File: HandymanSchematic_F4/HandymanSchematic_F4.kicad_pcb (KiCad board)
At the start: 4 copper layers, 60.5 x 94.5 mm, 81 parts, among them J1 SWD Header, J2 Footswitch, J3 TunerIn, J4 TuneThru, J5 GateIn, J6 GateOut, J7 PowerJack, Q1 BC847, Q2 2N7002, Q3 2N7002, SW1 RST, SW2 BYP, U1 SH1106, U2 TL074, U3 STM32F411RETx, U4 AMS1117, U6 TL072, Y1 16MHz

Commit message: noise schematic tweaks
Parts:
- removed R25: 100k, Resistor_SMD:R_0805_2012Metric
- removed U6: TL072, Package_SO:SOIC-8_3.9x4.9mm_P1.27mm
- added C2: 10u, Capacitor_SMD:C_0805_2012Metric, F.Cu at (88.9, 24.1)
- added C25: 2n2, Capacitor_SMD:C_0805_2012Metric, F.Cu at (88.9, 30.1)
- added C26: 470u, Capacitor_THT:CP_Radial_D6.3mm_P2.50mm, F.Cu at (100.9, 26.5)
- added C9: 10u, Capacitor_SMD:C_0805_2012Metric, F.Cu at (88.9, 27.1)
- added D2: BAT54S, Package_TO_SOT_SMD:SOT-23, F.Cu at (93.6, 24.8)
- added R11: 220, Resistor_SMD:R_0805_2012Metric, F.Cu at (84.5, 30.0)
- added R30: 1Meg, Resistor_SMD:R_0805_2012Metric, F.Cu at (84.5, 32.9)
- added R38: 470k, Resistor_SMD:R_0805_2012Metric, F.Cu at (84.5, 35.9)
- added R39: 4k7, Resistor_SMD:R_0805_2012Metric, F.Cu at (84.5, 38.8)
- added R4: 220, Resistor_SMD:R_0805_2012Metric, F.Cu at (84.5, 24.1)
- added R40: 22, Resistor_SMD:R_0805_2012Metric, F.Cu at (100.2, 31.9)
- added R6: 220, Resistor_SMD:R_0805_2012Metric, F.Cu at (84.5, 27.0)
- added U5: LM2904, Package_SO:SOIC-8_3.9x4.9mm_P1.27mm, F.Cu at (25.4, 13.7)
- R12, R8: value 470k -> 1Meg
- R13, R26: value 470k -> 100k
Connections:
- C1 pad 1: +9V -> +9VA
- C3 pad 1: +9V -> +9VA
- D4 pad 1: /Analog/AmpCathode -> Net-(D4-K)
- D7 pad 2: /Analog/AmpAnode -> Net-(D7-A)
- R1 pad 1: +9V -> +9VA
- R22 pad 2: Net-(C10-Pad1) -> Net-(R11-Pad1)
- R26 pad 2: TUNE_ADC -> Net-(R26-Pad2)
- R5 pad 1: +9V -> +9VA
- U2 pad 4: +9V -> +9VA
- U2 pad 8: Net-(C10-Pad1) -> Net-(R11-Pad1)

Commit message: layout
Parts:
- C26: moved to B.Cu
- moved D2 83.6 mm to (12.4, 4.80)
- moved C25 75.5 mm to (16.7, 8.03), turned to -90 degrees
- moved R39 71.2 mm to (20.3, 7.97), turned to 90 degrees
- moved R30 68.1 mm to (18.8, 15.1), turned to 90 degrees
- moved C2 66.6 mm to (22.5, 18.7), turned to -90 degrees
- moved R40 66.2 mm to (41.4, 1.70), turned to 90 degrees
- moved R38 65.3 mm to (22.5, 15.1), turned to 90 degrees
- moved R4 65.2 mm to (19.3, 26.5)
- moved C26 63.3 mm to (41.4, 4.95)
- moved R11 62.0 mm to (22.9, 37.0), turned to -90 degrees
- moved C9 59.8 mm to (29.8, 18.1), turned to -90 degrees
- moved R6 51.7 mm to (32.9, 23.6)
- moved R24 37.3 mm to (15.3, 15.0), turned to -90 degrees
- moved R28 31.4 mm to (16.7, 11.5), turned to -90 degrees
- moved R22 4.60 mm to (19.5, 33.6), turned to 0 degrees
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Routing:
- net +3.3V: track 290.6 -> 0.00 mm, vias 4 -> 0
- net +9V: track 157.3 -> 0.00 mm, vias 4 -> 0
- net /Digital/TunerModeIn: track 103.4 -> 0.00 mm, vias 2 -> 0
- net TUNE_IN: track 82.6 -> 0.00 mm, vias 1 -> 0
- net CLOSED_OUT: track 77.5 -> 0.00 mm, vias 2 -> 0
- net /Analog/VG: track 71.6 -> 0.00 mm, vias 2 -> 0
- net TUNE_THRU: track 58.9 -> 0.00 mm, vias 1 -> 0
- net Net-(C2-Pad1): track 55.3 -> 0.00 mm, vias 2 -> 0
- net NRST: track 46.6 -> 0.00 mm, vias 1 -> 0
- net LOOP_IN: track 40.5 -> 0.00 mm
- net /Digital/GateByp: track 36.5 -> 0.00 mm, vias 1 -> 0
- net RELEASE_IN: track 36.4 -> 0.00 mm, vias 1 -> 0
- net Net-(C11-Pad1): track 30.2 -> 0.00 mm
- net THRESH_IN: track 29.7 -> 0.00 mm, vias 1 -> 0
- net TUNE_ADC: track 27.8 -> 0.00 mm, vias 1 -> 0
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
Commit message: prelim routing
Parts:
- moved C9 0.93 mm to (28.9, 18.1)
- moved R19 0.36 mm to (16.0, 35.6), turned to 0 degrees
- moved C14 0.36 mm to (16.0, -4.65)
- moved R310 0.27 mm to (19.6, 3.30)
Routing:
- net +3.3V: track 0.00 -> 222.5 mm, vias 0 -> 6
- net /Digital/TunerModeIn: track 0.00 -> 92.0 mm, vias 0 -> 1
- net +9VA: track 0.00 -> 89.2 mm, vias 0 -> 2
- net TUNE_IN: track 0.00 -> 80.3 mm, vias 0 -> 1
- net CLOSED_OUT: track 0.00 -> 67.9 mm, vias 0 -> 2
- net /Analog/VG: track 0.00 -> 64.3 mm, vias 0 -> 3
- net +9V: track 0.00 -> 64.2 mm, vias 0 -> 2
- net TUNE_THRU: track 0.00 -> 55.9 mm
- net LOOP_IN: track 0.00 -> 55.5 mm
- net NRST: track 0.00 -> 48.0 mm, vias 0 -> 1
- net RELEASE_IN: track 0.00 -> 42.9 mm, vias 0 -> 1
- net +3.3VA: track 0.00 -> 42.5 mm, vias 0 -> 2
- net /Digital/GateByp: track 0.00 -> 36.1 mm, vias 0 -> 2
- net THRESH_IN: track 0.00 -> 35.0 mm, vias 0 -> 1
- net /Analog/SumPt: track 0.00 -> 30.3 mm, vias 0 -> 2
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
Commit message: wider jack spacing, DRC passing
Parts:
- moved J8 0.34 mm to (53.0, 13.9)
- moved J4 0.28 mm to (18.5, 22.7)
- moved J6 0.28 mm to (18.5, 43.8)
- moved J3 0.15 mm to (37.2, 38.9)
- moved J5 0.15 mm to (37.2, 60.0)
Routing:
- net LOOP_IN: track 55.5 -> 53.6 mm
- net GND: vias 63 -> 69

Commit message: stitching vias, trace improvements
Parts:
- moved C11 0.37 mm to (40.6, 36.6)
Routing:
- net TUNE_IN: track 80.3 -> 85.6 mm
- net NRST: track 48.0 -> 51.5 mm
- net /Analog/AmpCathode: track 19.5 -> 17.5 mm, vias 2 -> 0
- net TUNE_THRU: track 55.9 -> 54.3 mm
- net /Digital/DISP_SDA: track 26.5 -> 27.7 mm
- net /Digital/TunerModeIn: track 91.8 -> 92.4 mm
- net /Digital/GateByp: track 36.1 -> 36.3 mm, vias 2 -> 1
- net GND: vias 69 -> 74

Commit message: rev7 ready for fab
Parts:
- moved R3 8.95 mm to (53.0, 26.9)
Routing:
- net +9VA: track 89.1 -> 73.8 mm, vias 2 -> 3
- net THRESH_IN: track 35.0 -> 29.7 mm
- net NRST: track 51.5 -> 49.8 mm
- net CLOSED_OUT: track 67.9 -> 69.5 mm
- net +9V: track 64.2 -> 65.6 mm
- net Net-(Q1-B): track 7.67 -> 6.61 mm
- net +3.3VA: track 42.5 -> 43.1 mm
- net GND: vias 74 -> 80
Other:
- board text added: "Rev 7- 10/2026 Hayden Setlik"
- board text removed: "Rev 6- 08/2026 Hayden Setlik"

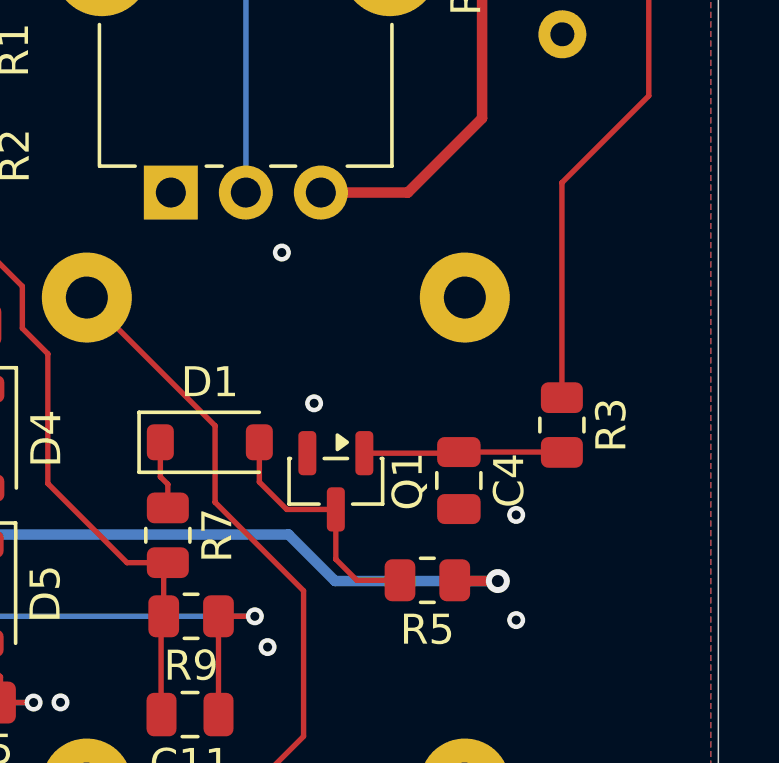
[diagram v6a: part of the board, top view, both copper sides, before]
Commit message: switched to FET controlled gate circuit
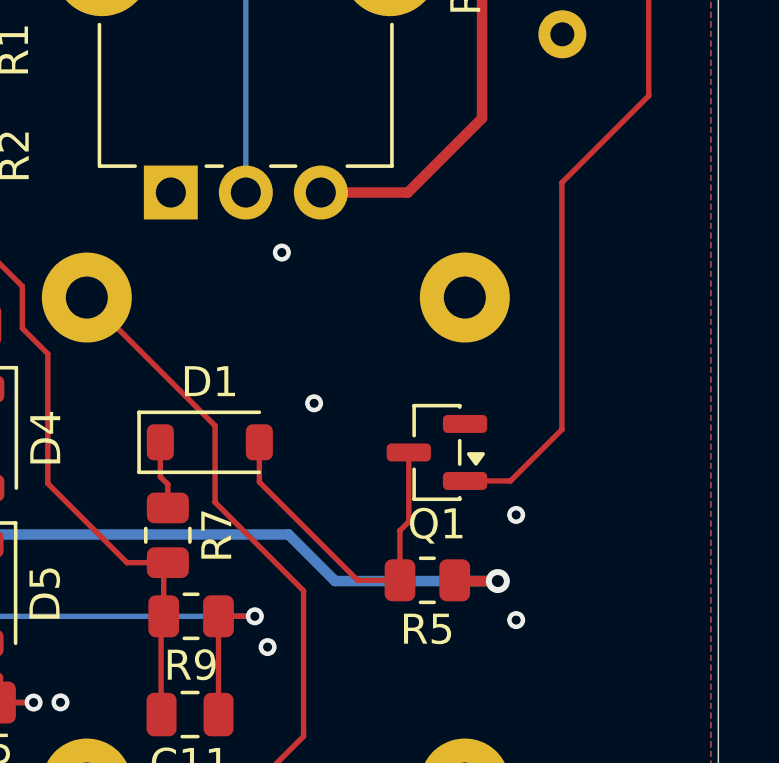
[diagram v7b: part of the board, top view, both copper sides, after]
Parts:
- removed C4: 100n, Capacitor_SMD:C_0805_2012Metric
- removed R3: 10k, Resistor_SMD:R_0805_2012Metric
- Q1: value BC847 -> 2N7002
- moved Q1 3.50 mm to (48.9, 27.8), turned to 180 degrees
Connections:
- Q1 pad 1: Net-(Q1-B) -> CLOSED_OUT
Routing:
- net Net-(Q1-B): track 6.61 -> 0.00 mm
- net CLOSED_OUT: track 69.5 -> 74.5 mm
- net Net-(D1-A): track 8.34 -> 11.8 mm

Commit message: rev7 ready for fab
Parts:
- moved D2 1.49 mm to (13.6, 3.81)
- moved R6 0.41 mm to (32.5, 23.6)
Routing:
- net Net-(U5A-+): track 21.6 -> 19.8 mm
- net +3.3VA: track 43.1 -> 43.6 mm
- net GND: vias 80 -> 78
